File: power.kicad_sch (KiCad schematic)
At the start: 31 parts, among them J501 694106301002, U501 LMR50410, U502 TLV1117-50, U503 TLV74133PDBVR

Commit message: Working on schematic
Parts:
- added D502: ZMM5242B, Diode_SMD:D_MiniMELF, symbol Device:D_Zener_Small
- added Q501: DMG2307LQ, Package_TO_SOT_SMD:SOT-23, symbol Device:Q_PMOS_GSD
- added R508: 10k, Resistor_SMD:R_0805_2012Metric_Pad1.20x1.40mm_HandSolder, symbol Device:R_Small
- C503, C506: footprint (none) -> Capacitor_SMD:C_0805_2012Metric_Pad1.18x1.45mm_HandSolder
- R501, R502, R504, R505: footprint (none) -> Resistor_SMD:R_0805_2012Metric_Pad1.20x1.40mm_HandSolder
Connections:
- net +5V: now also D501.3 (common)
- net +5VA: no longer D501.3 (common)
- net +6V: now also D501.2 (K)
- net +VDC: now also D502.1 (K), Q501.2 (S); no longer D501.2 (K), J501.1
- net GND: now also R508.2
- new net: J501.1, Q501.3 (D)
- new net: D502.2 (A), Q501.1 (G), R508.1
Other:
- moved on the sheet: C501, C502, C503, C504, C505, C506, C507, C508, C509, C510, C511, FB501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

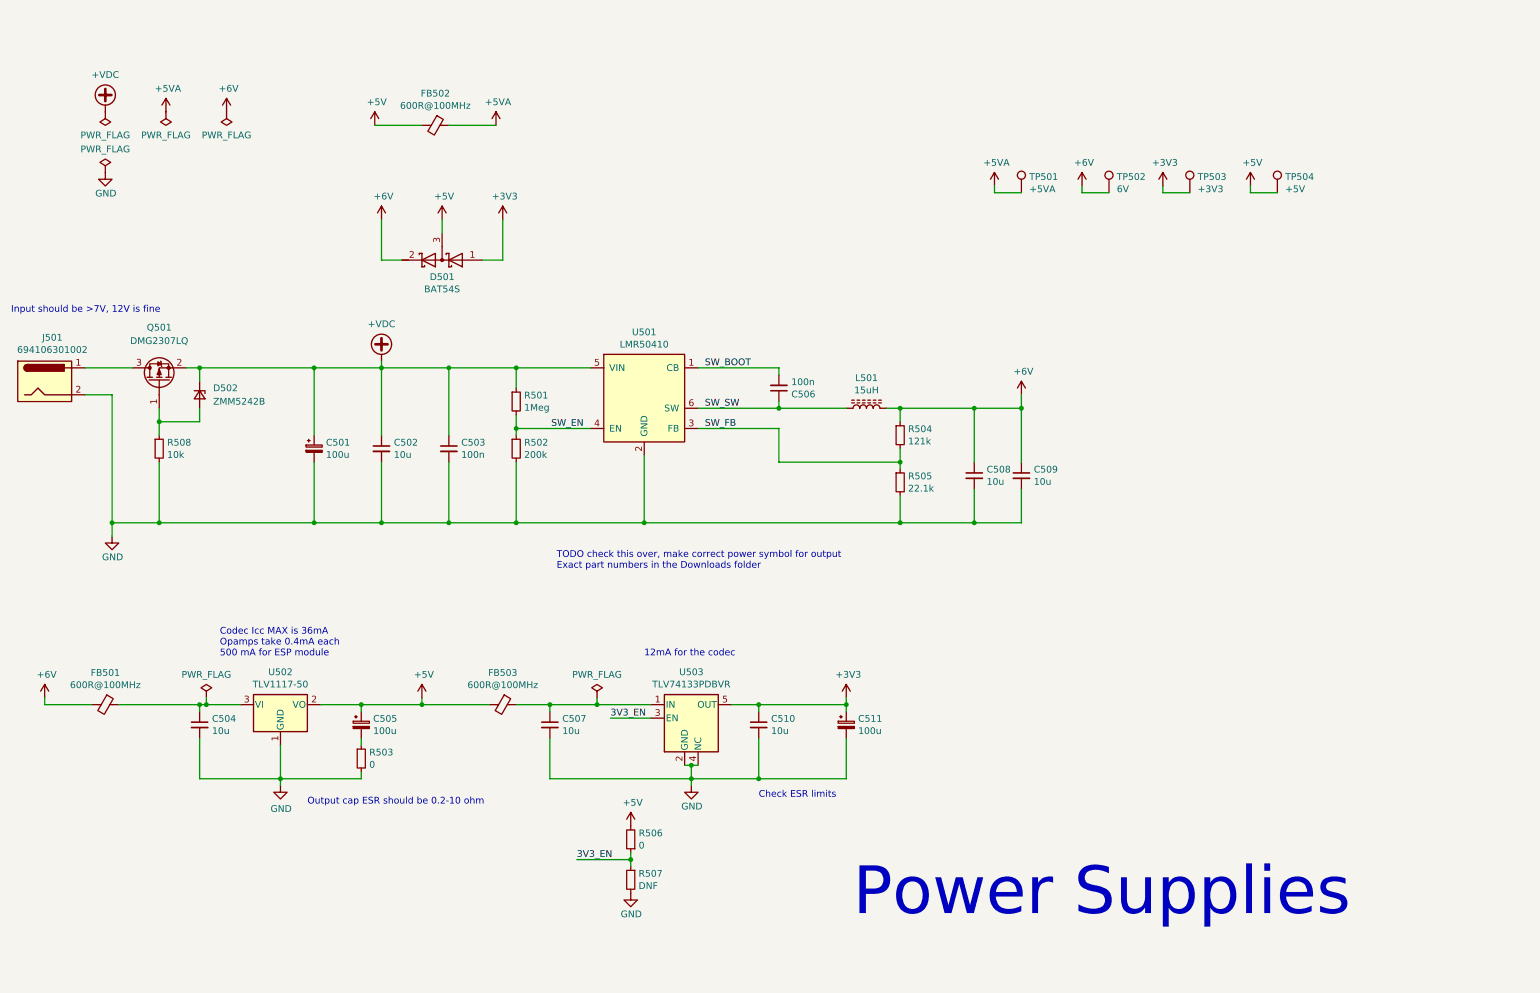
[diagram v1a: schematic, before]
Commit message: Review PSU, add footprints for all components
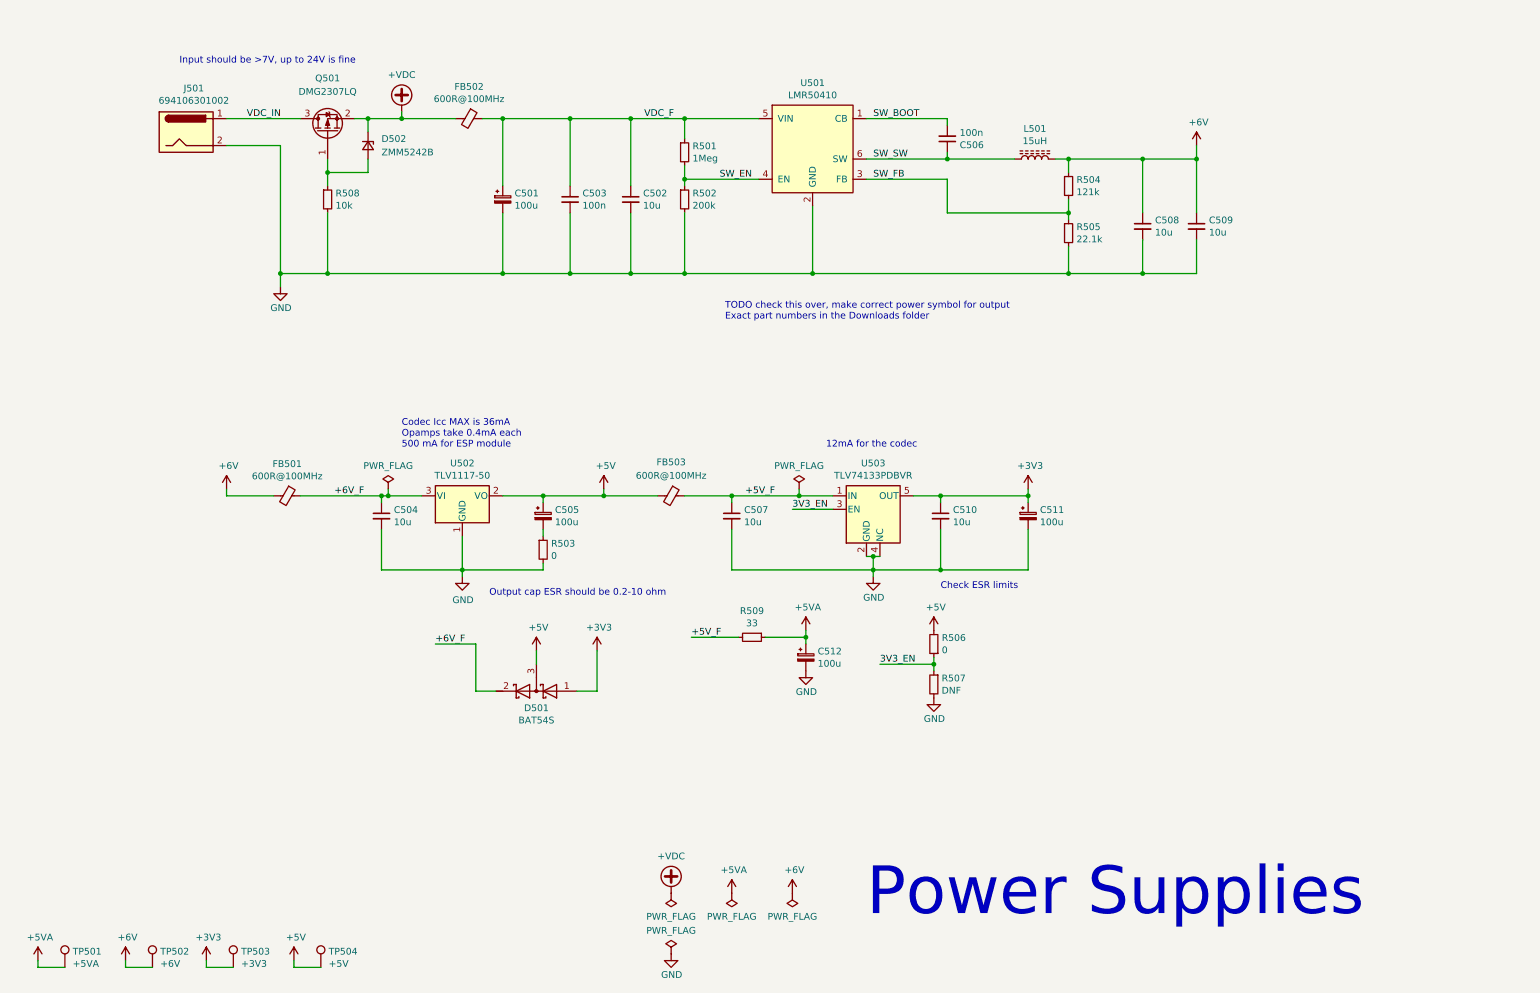
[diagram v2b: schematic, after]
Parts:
- added C512: 100u, Capacitor_SMD:CP_Elec_6.3x7.7, symbol Device:CP_Small
- added R509: 33, Resistor_SMD:R_0805_2012Metric_Pad1.20x1.40mm_HandSolder, symbol Device:R_Small
- C502, C504, C507, C508, C509, C510: footprint (none) -> Capacitor_SMD:C_1206_3216Metric_Pad1.33x1.80mm_HandSolder; PN (none) -> GMK316AB7106KL-TR
- C503, C506: PN (none) -> C0805C104M3RACTU
- D502: PN (none) -> ZMM5242B
- L501: footprint (none) -> Inductor_SMD:L_Bourns-SRN8040_8x8.15mm; PN (none) -> NRS8040T150MJGJ
- TP502: value 6V -> +6V
- U501: PN (none) -> LMR50410XFDBVR
- U502: footprint Package_TO_SOT_THT:TO-220-3_Vertical -> Package_TO_SOT_SMD:SOT-223-3_TabPin2; PN (none) -> TLV1117-15CDCY
- U503: footprint Package_TO_SOT_THT:TO-220-3_Vertical -> Package_TO_SOT_SMD:SOT-23-5; PN (none) -> TLV74133PDBVR
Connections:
- net +5V: no longer FB502.2
- net +5VA: now also C512.1, R509.1; no longer FB502.1
- net +6V: no longer D501.2 (K)
- net +VDC: now also FB502.2; no longer C501.1, C502.1, C503.1, R501.1, U501.5 (VIN)
- net GND: now also C512.2
- net +5V_F: now reaches C507.1, FB503.1, U503.1 (IN)
- net +5V_F: now also R509.2
- net VDC_IN: now reaches J501.1, Q501.3 (D)
- net +6V_F: now reaches C504.1, FB501.1, U502.3 (VI)
- net +6V_F: now also D501.2 (K)
- new net VDC_F: C501.1, C502.1, C503.1, FB502.1, R501.1, U501.5 (VIN)
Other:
- note added: "Input should be >7V, up to 24V is fine"
- note removed: "Input should be >7V, 12V is fine"
- moved on the sheet: C501, C502, C503, C504, C505, C506, C507, C508, C509, C510, C511, D501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

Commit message: Tweak layout
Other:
- note removed: "TODO check this over, make correct power symbol for output Exact part numbers in the Downloads folder"
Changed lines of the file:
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@@
-    (effects (font (size 1.27 1.27)) (justify left bottom))
-  )
-  (text "TODO check this over, make correct power symbol for output\nExact part numbers in the Downloads folder"
-    (at 153.67 68.58 0)
     (effects (font (size 1.27 1.27)) (justify left bottom))
   )

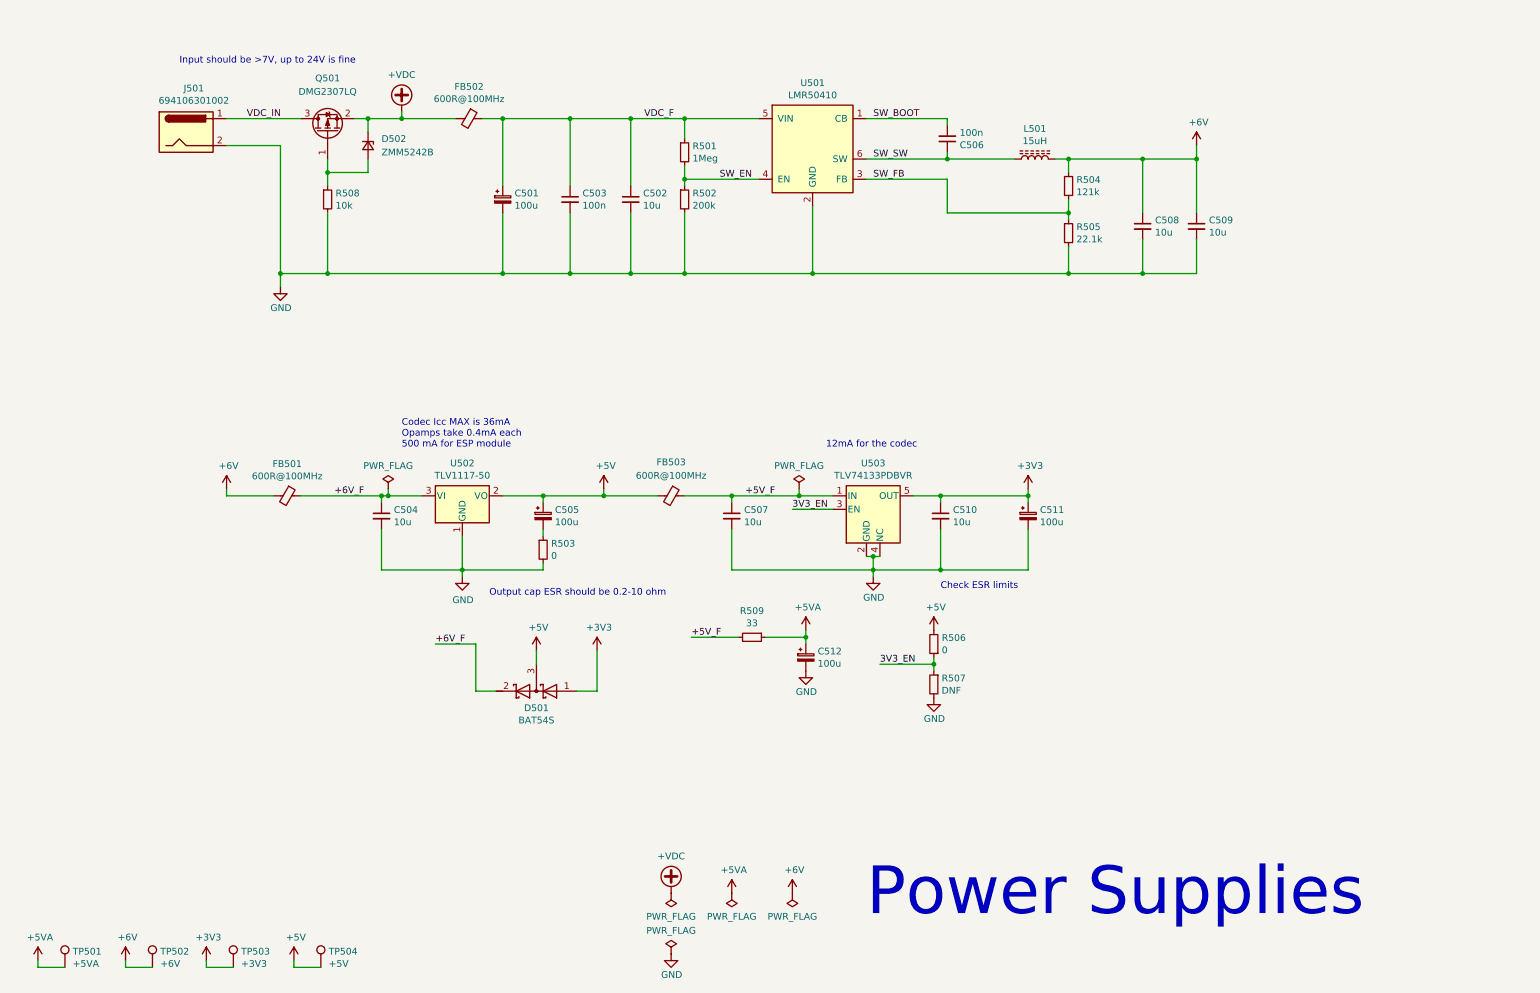
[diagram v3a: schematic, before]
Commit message: Schematic reviewed, assign PN to all parts
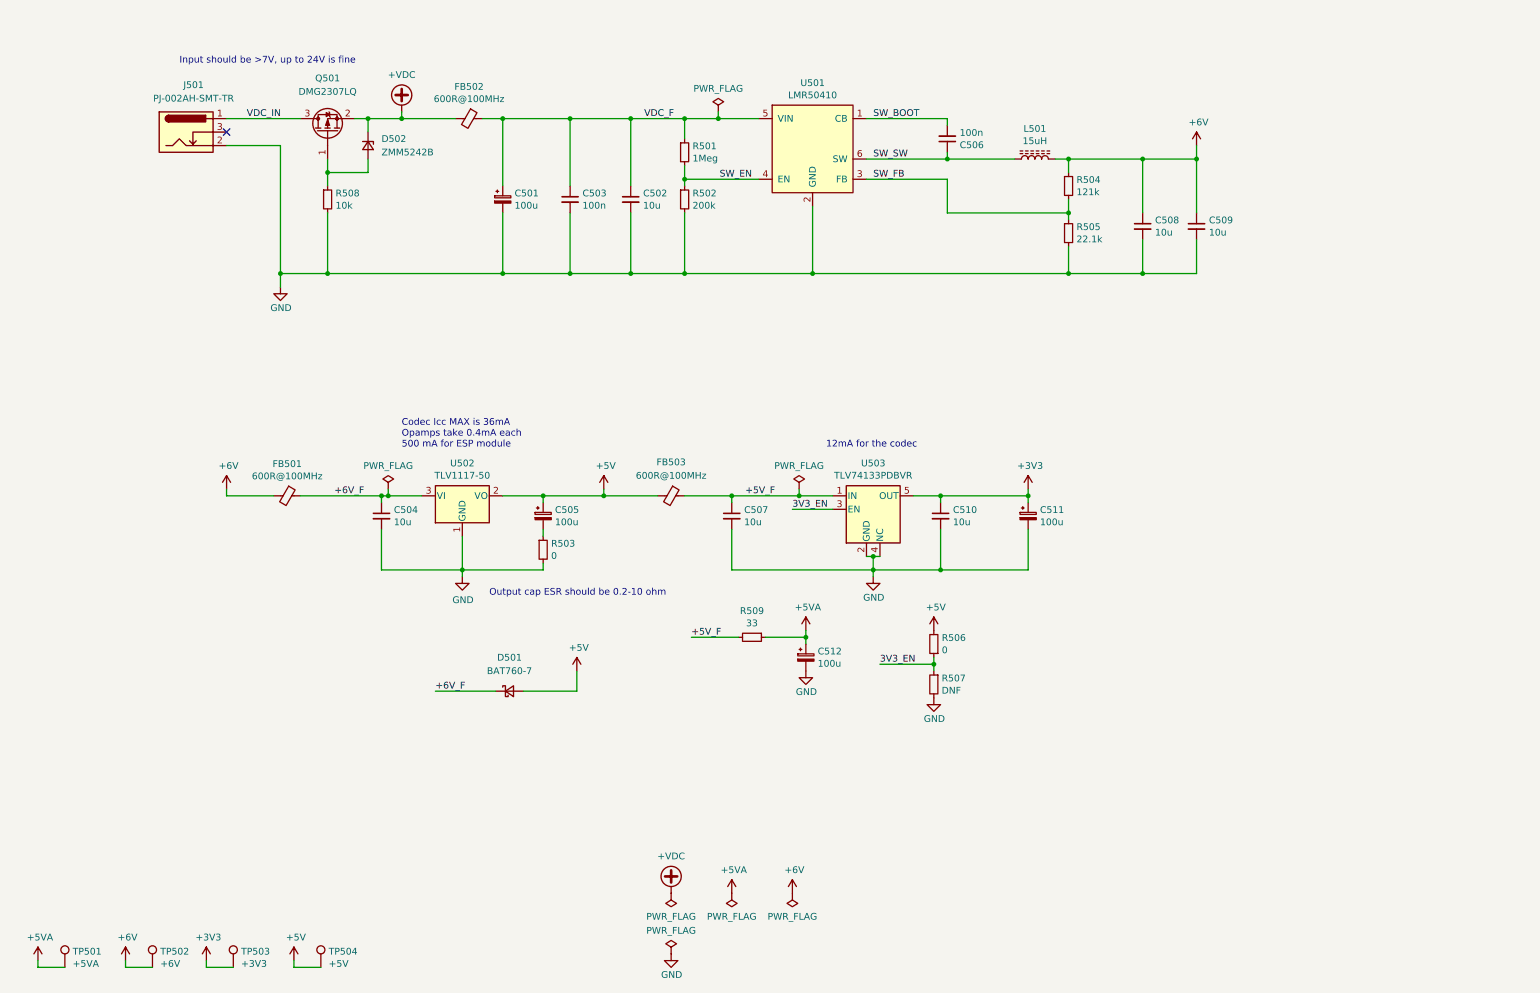
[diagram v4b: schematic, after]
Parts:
- removed D501: BAT54S, Package_TO_SOT_SMD:SOT-23, symbol Device:D_Schottky_x2_Serial_AKC
- removed J501: 694106301002, Connector_BarrelJack:BarrelJack_Wuerth_6941xx301002, symbol Connector:Barrel_Jack
- added D501: BAT760-7, Diode_SMD:D_SOD-323_HandSoldering, symbol Device:D_Schottky_Small
- added J501: PJ-002AH-SMT-TR, guitar_dsp_platform:CUI_PJ-002AH-SMT-TR, symbol Connector:Barrel_Jack_Switch
- R501: PN (none) -> CR0805-FX-1004ELF
- R502: PN (none) -> CR0805-FX-2003ELF
- R503, R506: PN (none) -> CR0805-J/-000ELF
- R504: PN (none) -> CR0805-FX-1213ELF
- R505: PN (none) -> CR0805-FX-2212ELF
- R507, TP501, TP502, TP503, TP504: now left out of the parts list
- R508: PN (none) -> CR0805-FX-1002ELF
- R509: PN (none) -> CR0805-FX-33R0ELF
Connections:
- net +5V: now also D501.2 (A)
- net +6V_F: now also D501.1 (K)
- net GND: now also J501.2
- net VDC_IN: now also J501.1
- no-connect marks 0 -> 1
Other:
- note removed: "Check ESR limits"
- note removed: "Power Supplies"

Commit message: Start BOM tidy up
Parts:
- D502: value ZMM5242B -> TZMC12-GS08; PN ZMM5242B -> TZMC12-GS08
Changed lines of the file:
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@@
       (effects (font (size 1.27 1.27)) (justify left))
     )
-    (property "Value" "ZMM5242B" (id 1) (at 88.9 36.8299 90)
+    (property "Value" "TZMC12-GS08" (id 1) (at 88.9 36.8299 90)
       (effects (font (size 1.27 1.27)) (justify left))
     )
@@
       (effects (font (size 1.27 1.27)) hide)
     )
-    (property "Datasheet" "https://www.mouser.co.uk/datasheet/2/345/zmm52xxb-34158.pdf" (id 3) (at 86.36 35.56 90)
+    (property "Datasheet" "https://www.vishay.com/docs/84122/tzm.pdf" (id 3) (at 86.36 35.56 90)
       (effects (font (size 1.27 1.27)) hide)
     )
-    (property "PN" "ZMM5242B" (id 4) (at 86.36 35.56 0)
+    (property "PN" "TZMC12-GS08" (id 4) (at 86.36 35.56 0)
       (effects (font (size 1.27 1.27)) hide)
     )
